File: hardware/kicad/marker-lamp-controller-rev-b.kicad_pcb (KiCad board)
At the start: 2 copper layers, 80 x 45 mm, 21 parts, among them J1 TBP01R1-508-04BE, Q1 BC807-40, U1 BSP762TXUMA1, U2 VO617A-4X017T

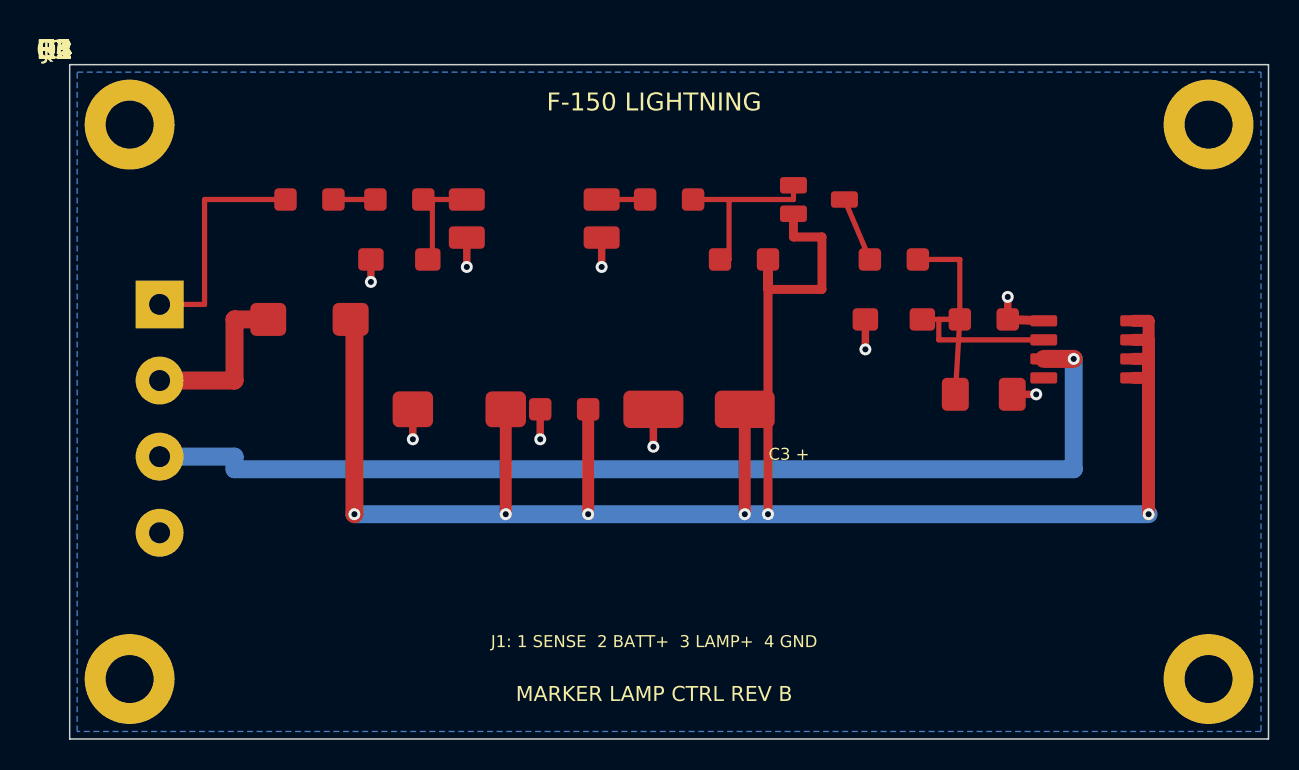
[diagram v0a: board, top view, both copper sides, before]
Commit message: Add hand-assembly silkscreen markings
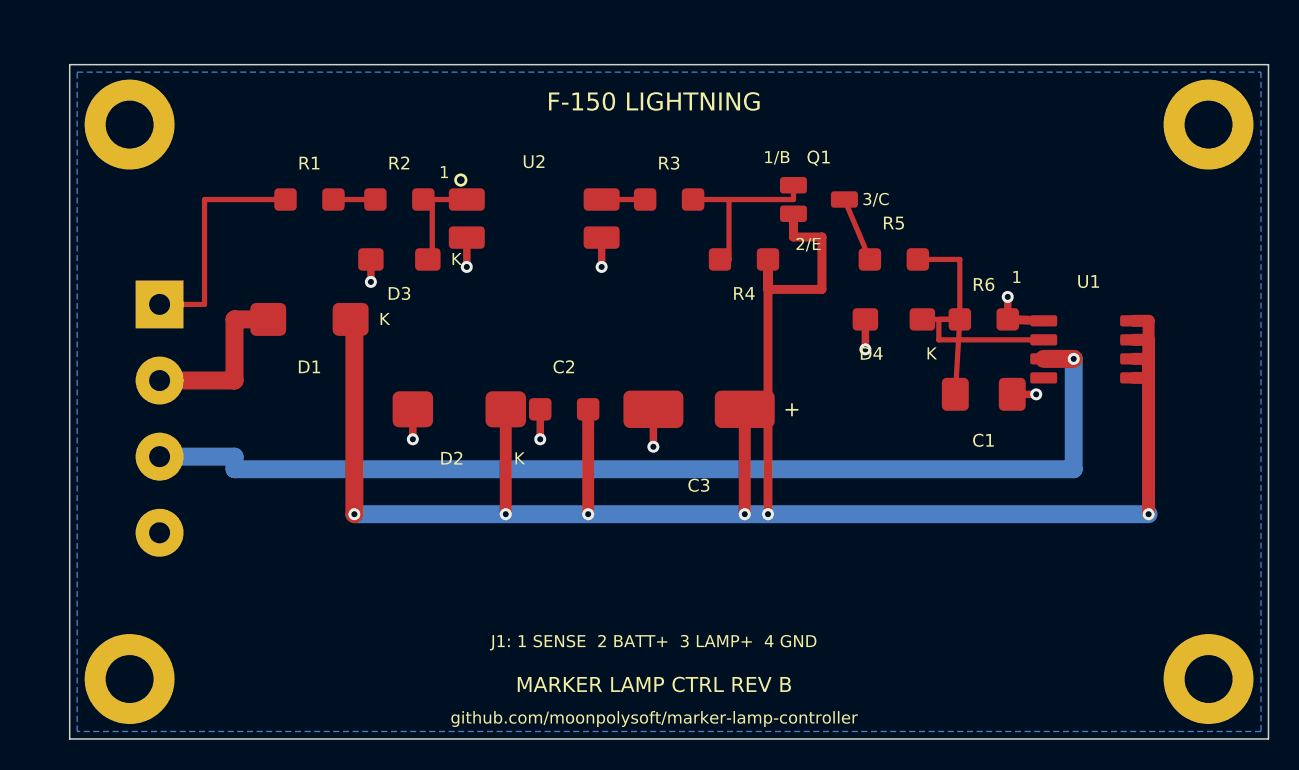
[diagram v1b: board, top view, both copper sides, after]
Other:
- board text added: "+"
- board text added: "1"
- board text added: "1/B"
- board text added: "2/E"
- board text added: "3/C"
- board text added: "C1"
- board text added: "C2"
- board text added: "C3"
- board text added: "D1"
- board text added: "D2"
- board text added: "D3"
- board text added: "D4"
- board text added: "K"
- board text added: "Q1"
- board text added: "R1"
- board text added: "R2"
- board text added: "R3"
- board text added: "R4"
- board text added: "R5"
- board text added: "R6"
- board text added: "U1"
- board text added: "U2"
- board text added: "github.com/moonpolysoft/marker-lamp-controller"
- board text removed: "C3 +"
